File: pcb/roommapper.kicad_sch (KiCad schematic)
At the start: 3 parts, among them U1 STM32F411CEUx_BlackPill, U2 RPLIDAR_C1

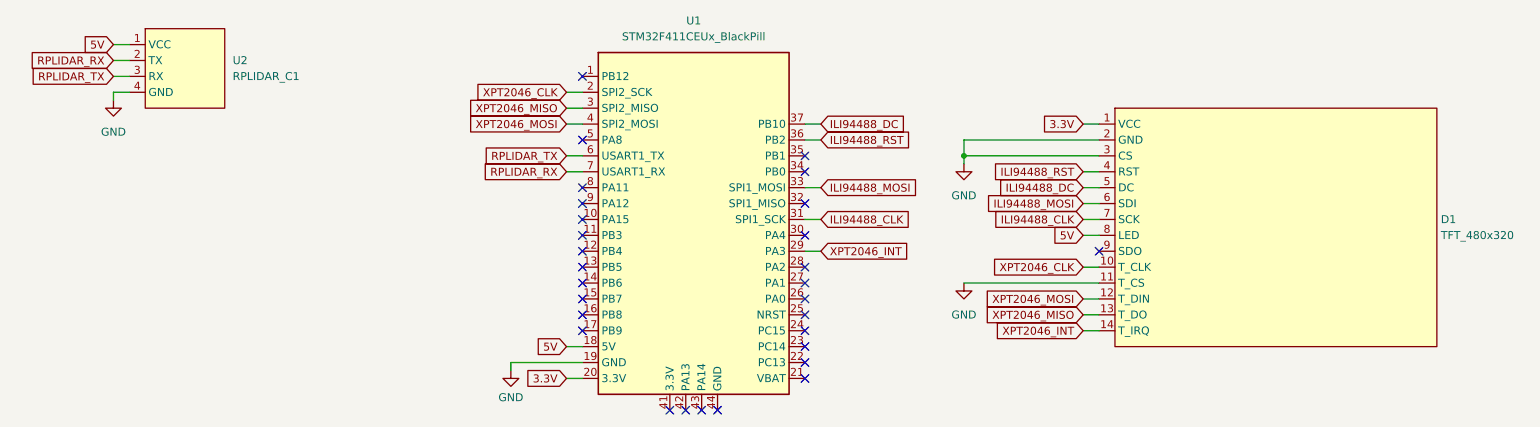
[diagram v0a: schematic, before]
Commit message: general: update project io pins for easier pcb routing
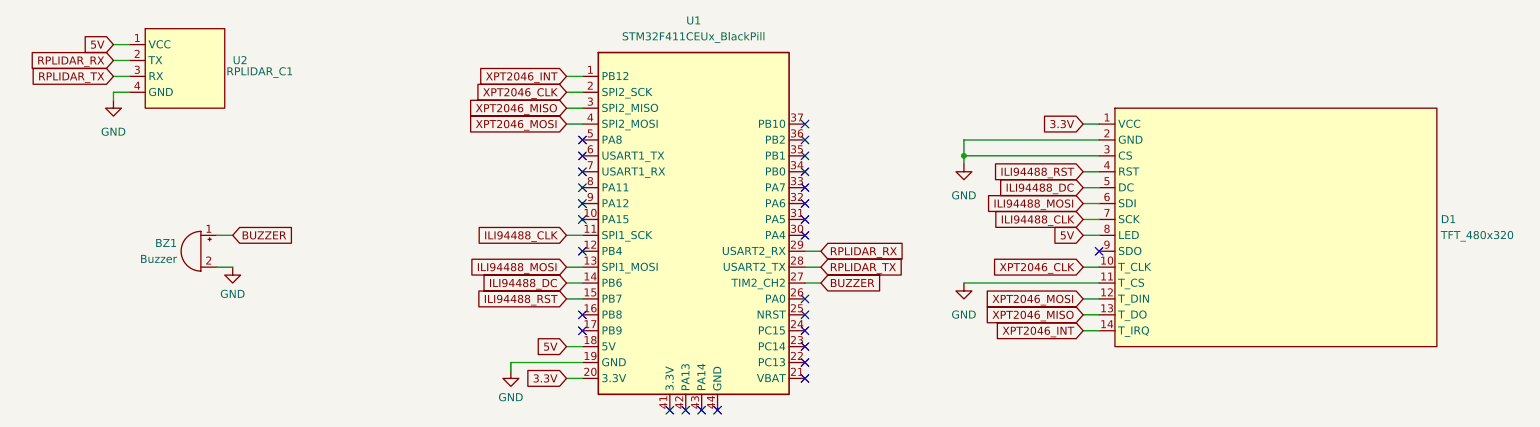
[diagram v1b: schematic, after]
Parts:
- added BZ1: Buzzer, Buzzer_Beeper:Buzzer_D14mm_H7mm_P10mm, symbol Device:Buzzer
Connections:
- net GND: now also BZ1.2 (-)
- net ILI94488_CLK: now also U1.11 (PB3); no longer U1.31 (PA5)
- net ILI94488_DC: now also U1.14 (PB6); no longer U1.37 (PB10)
- net ILI94488_MOSI: now also U1.13 (PB5); no longer U1.33 (PA7)
- net ILI94488_RST: now also U1.15 (PB7); no longer U1.36 (PB2)
- net RPLIDAR_RX: now also U1.29 (PA3); no longer U1.7 (PA10)
- net RPLIDAR_TX: now also U1.28 (PA2); no longer U1.6 (PA9)
- net XPT2046_INT: now also U1.1 (PB12); no longer U1.29 (PA3)
- net BUZZER: now reaches U1.27 (PA1)
- net BUZZER: now also BZ1.1 (+)
- no-connect marks 29 -> 28
